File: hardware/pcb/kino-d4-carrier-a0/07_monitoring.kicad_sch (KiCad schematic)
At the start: 10 parts, among them U700 PAC1954T-E/4MX, U701 BQ27441DRZR-G1A

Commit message: fix(hardware): carrier A0.2 - U700 pin 1 triangle off C700's pad
The stock VQFN-16 pin 1 triangle sits 0.3 mm beyond pin 1, on C700's
pad 1 (ODD JOBS 94). U700 now uses a project footprint with the same land
and the triangle in the free corner beside pin 1 (fp_a02_pac1954.py);
capture, BOM, netlist, ERC (0) and PDF regenerated. No footprint/library
mismatch on the board.

Co-Authored-By: Claude Opus 5.5 <noreply@anthropic.com>
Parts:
- U700: footprint Package_DFN_QFN:VQFN-16-1EP_3x3mm_P0.5mm_EP1.1x1.1mm -> KINO_A0:VQFN-16-1EP_3x3mm_P0.5mm_EP1.1x1.1mm_Pin1Corner
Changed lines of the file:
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@@
                   (property "Reference" "U700" (at 73.66 43.25999999999999 0) (effects (font (size 1.27 1.27))))
                   (property "Value" "PAC1954T-E/4MX" (at 73.66 45.75999999999999 0) (effects (font (size 1.0 1.0))))
-                  (property "Footprint" "Package_DFN_QFN:VQFN-16-1EP_3x3mm_P0.5mm_EP1.1x1.1mm" (at 73.66 60.959999999999994 0) (effects (font (size 1 1)) (hide yes)))
+                  (property "Footprint" "KINO_A0:VQFN-16-1EP_3x3mm_P0.5mm_EP1.1x1.1mm_Pin1Corner" (at 73.66 60.959999999999994 0) (effects (font (size 1 1)) (hide yes)))
                   (property "Datasheet" "https://ww1.microchip.com/downloads/en/DeviceDoc/PAC195X-Data-Sheet-20006539.pdf" (at 73.66 60.959999999999994 0) (effects (font (size 1 1)) (hide yes)))
                   (property "Design note" "ADDRSEL grounded gives 7-bit 0x10 (Microchip evaluation guide section 4.6). PWRDN high enables; SLOW low gives default sample rate." (at 73.66 60.959999999999994 0) (effects (font (size 1 1)) (hide yes)))

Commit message: feat(hardware): carrier A0.2 - I2C into U700, ADDRSEL strap dropped
U700's SCL and SDA pins were walled in by C700's MB_3V3 link, C701 and
PAC_ADDR's run to the R700 strap. R700 (0 ohm ADDRSEL to GND, address
0x10) leaves the capture: U700 is the only PAC1954 on the bus, so pin 6
ties to the exposed GND pad. C701 turns and moves west, the MB_3V3 trunk
reaches pin 16's via directly. SCL runs on In2 along the free corridor
north of camera 2's header into the SCL bundle; SDA goes down the free
In2 column between the SYS_5V riser and camera 3's socket towards U800.
Capture, BOM, netlist, ERC (0), PDF regenerated. 42 -> 41 open; no
clearance or short errors.

Co-Authored-By: Claude Opus 5.5 <noreply@anthropic.com>
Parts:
- removed R700: 0, Resistor_SMD:R_0603_1608Metric, symbol KINO_A0:R700
- U700: Design note ADDRSEL grounded gives 7-bit 0x10 (Microchip evaluation gui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 -> ADDRSEL tied to GND (pin 6 to the exposed pad) gives 7-bit 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
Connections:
- net PAC_ADDR is gone; now on net GND: U700.6 (ADDRSEL)
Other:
- moved on the sheet: C700, C701, C702, C703, R701, R702, RS700, U701

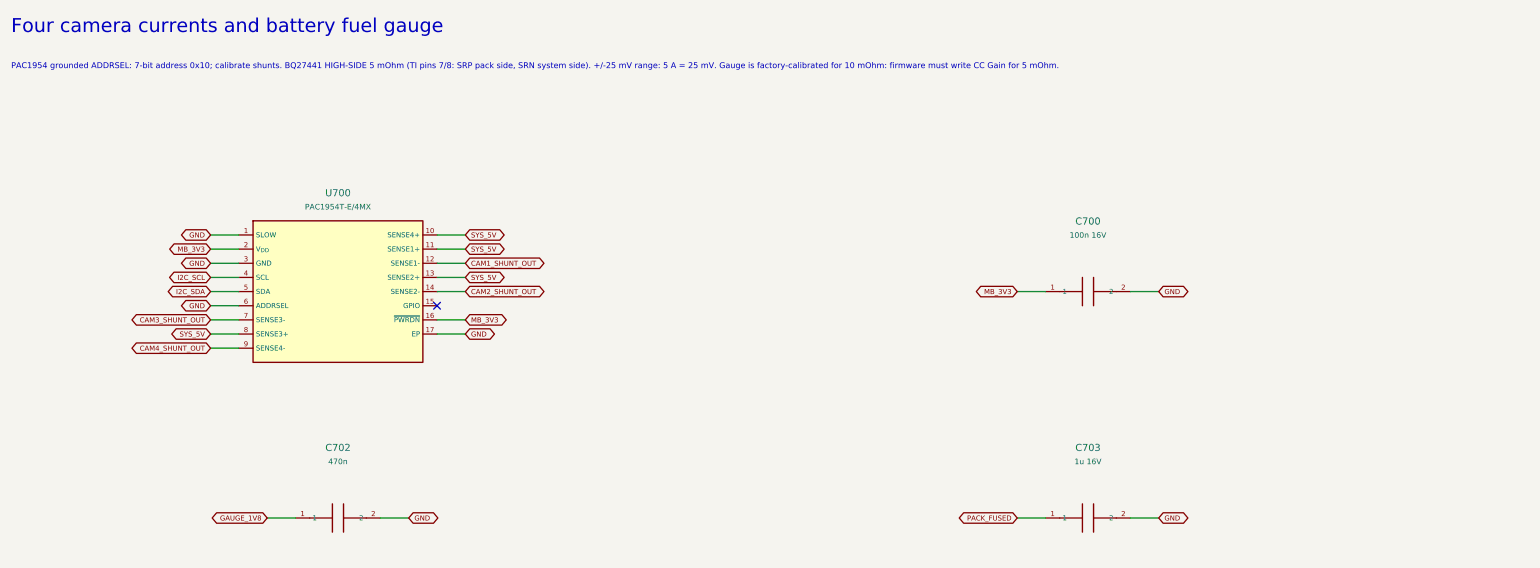
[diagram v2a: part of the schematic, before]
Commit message: feat(hardware): carrier A0.2 release pass - ready for fabrication with manual checks
Release review of the routed A0.2 carrier (A02-RELEASE.md: release matrix,
manual checks before ordering, bring-up tests). Final status: READY FOR
FABRICATION WITH SPECIFIC MANUAL CHECKS.

- USB-C input survives an unprogrammed STUSB4500 (20 V): D1001 SMF22A,
  R1004 10k, PD and load-switch P-FETs AO4409.
- Boost enable: R1204 100k BOOST_ENABLE to SYS_RAW (LTC2955-1 EN is a 2 uA
  source), Q1202 PMV16UN.
- I2C buffer U100 sides swapped (local bus on the TCA9517 A side's hard
  low); R100/R101 2.2k/22k hold EN low with JP1 pin 1 open.
- R105 SYNC_MASTER pull-down; D903 ESD on FN_N; TP1001 removed.
- SYS_RAW battery path as B.Cu and In2 pours with 25 extra vias; 1 oz inner
  copper in the stackup.
- XIAO socket pads get their solder-mask openings (footprint generator bug).
- Three fiducials per face; vias out of and away from pads; U1200 outline and
  pin-1 mark; legend lines and strokes 0.15 mm; silk association pass;
  CARRIER A0.2 / 2026-10 / S/N marking.
- Fab package (fab_a02.py): Gerbers + job file, drill, zip, placement files,
  fab BOM matched to LCSC by part number, hand-fit socket list, fab notes.
- Firmware constants header kino_carrier_a02.h.

DRC 0 / unconnected 0, ERC 0, verify.py --a02 passes.

Co-Authored-By: Claude Opus 5.5 <noreply@anthropic.com>
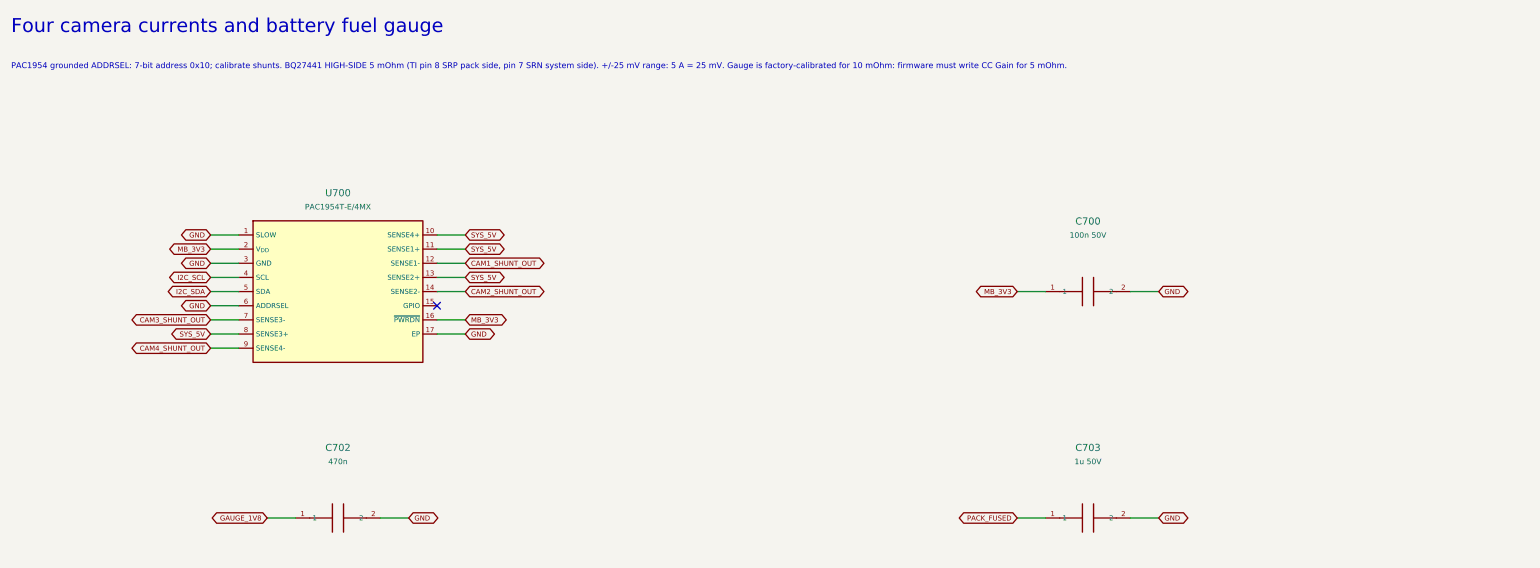
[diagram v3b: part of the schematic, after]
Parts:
- C700: value 100n 16V -> 100n 50V
- C703: value 1u 16V -> 1u 50V
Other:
- note added: "PAC1954 grounded ADDRSEL: 7-bit address 0x10; calibrate shunts. BQ27441 HIGH-SIDE 5 mOhm (TI pin 8 SRP pack side, pin 7 SRN system side). +/-25 mV range: 5 A = 25 mV. Gauge is factory-calibrated for 10 mOhm: firmware must write CC Gain for 5 mOhm."
- note removed: "PAC1954 grounded ADDRSEL: 7-bit address 0x10; calibrate shunts. BQ27441 HIGH-SIDE 5 mOhm (TI pins 7/8: SRP pack side, SRN system side). +/-25 mV range: 5 A = 25 mV. Gauge is factory-calibrated for 10 mOhm: firmware must write CC Gain for 5 mOhm."
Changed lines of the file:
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@@
       (company "KINO") (comment 1 "ENGINEERING DRAFT - NOT FOR FABRICATION"))
 (text "Four camera currents and battery fuel gauge" (at 15 12 0) (effects (font (size 2.5 2.5)) (justify left top)))
-(text "PAC1954 grounded ADDRSEL: 7-bit address 0x10; calibrate shunts. BQ27441 HIGH-SIDE 5 mOhm (TI pins 7/8: SRP pack side, SRN system side). +/-25 mV range: 5 A = 25 mV. Gauge is factory-calibrated for 10 mOhm: firmware must write CC Gain for 5 mOhm." (at 15 20 0) (effects (font (size 1.05 1.05)) (justify left top)))
+(text "PAC1954 grounded ADDRSEL: 7-bit address 0x10; calibrate shunts. BQ27441 HIGH-SIDE 5 mOhm (TI pin 8 SRP pack side, pin 7 SRN system side). +/-25 mV range: 5 A = 25 mV. Gauge is factory-calibrated for 10 mOhm: firmware must write CC Gain for 5 mOhm." (at 15 20 0) (effects (font (size 1.05 1.05)) (justify left top)))
 (symbol (lib_id "KINO_A0:U700") (at 73.66 60.959999999999994 0) (unit 1)
                   (in_bom yes) (on_board yes) (dnp no)
@@
                   (in_bom yes) (on_board yes) (dnp no)
                   (property "Reference" "C700" (at 208.28 48.339999999999996 0) (effects (font (size 1.27 1.27))))
-                  (property "Value" "100n 16V" (at 208.28 50.839999999999996 0) (effects (font (size 1.0 1.0))))
+                  (property "Value" "100n 50V" (at 208.28 50.839999999999996 0) (effects (font (size 1.0 1.0))))
                   (property "Footprint" "Capacitor_SMD:C_0603_1608Metric" (at 208.28 60.959999999999994 0) (effects (font (size 1 1)) (hide yes)))
                   (property "Datasheet" "https://www.yageogroup.com/component-documentation/download/specsheet/CC0603KRX7R9BB104" (at 208.28 60.959999999999994 0) (effects (font (size 1 1)) (hide yes)))
@@
                   (in_bom yes) (on_board yes) (dnp no)
                   (property "Reference" "C703" (at 208.28 88.98 0) (effects (font (size 1.27 1.27))))
-                  (property "Value" "1u 16V" (at 208.28 91.48 0) (effects (font (size 1.0 1.0))))
+                  (property "Value" "1u 50V" (at 208.28 91.48 0) (effects (font (size 1.0 1.0))))
                   (property "Footprint" "Capacitor_SMD:C_0603_1608Metric" (at 208.28 101.60000000000001 0) (effects (font (size 1 1)) (hide yes)))
                   (property "Datasheet" "" (at 208.28 101.60000000000001 0) (effects (font (size 1 1)) (hide yes)))
